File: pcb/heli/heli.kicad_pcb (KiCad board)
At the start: 4 copper layers, 50.6 x 50 mm, 68 parts, among them J1 Batterie, J2 Debug, J4 Servo, J5 Servo, M1 Motor_DC, M2 Motor_DC, Q1 IRLZ44N, Q2 BC547, Q3 IRLZ44N, Q4 BC547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

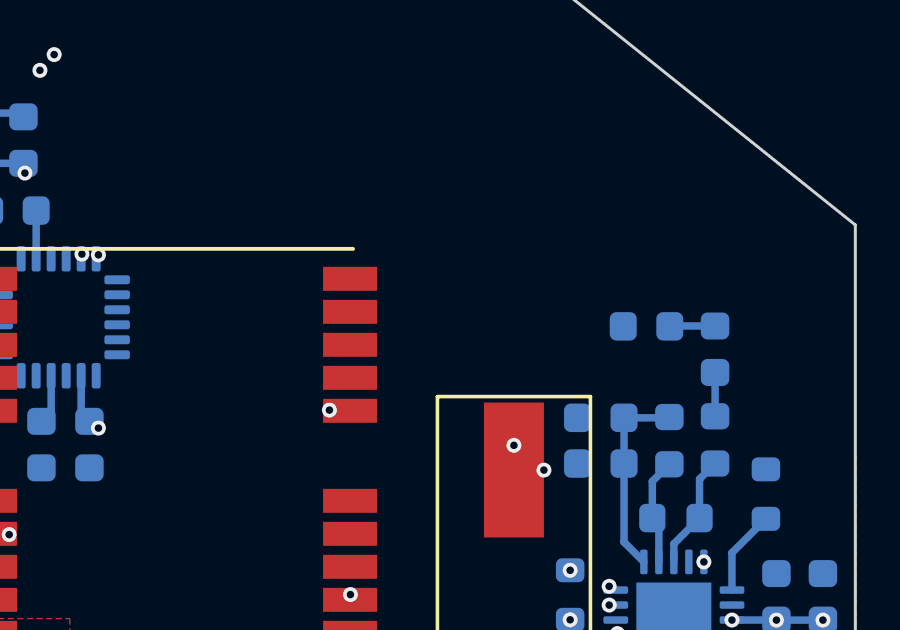
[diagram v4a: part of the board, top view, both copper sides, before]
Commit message: 
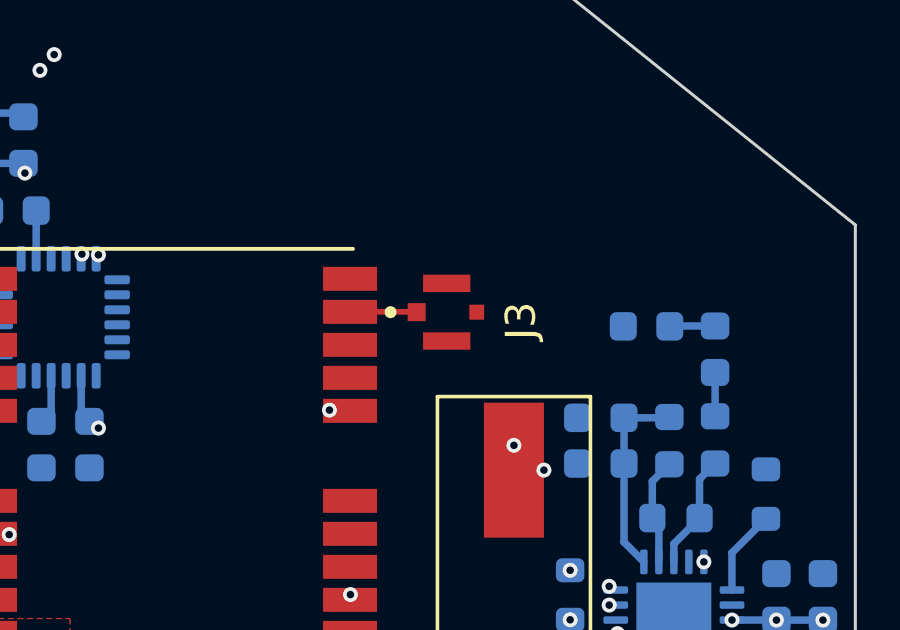
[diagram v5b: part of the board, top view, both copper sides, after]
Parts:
- added J3: CONMHF4-SMD-G-T, lib:LINX_CONMHF4-SMD-G-T, F.Cu at (55.0, 32.8)
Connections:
- U4 pad 11: unconnected-(U4-Pad11) -> Net-(J3-Pad1)
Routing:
- net Net-(J3-Pad1): track 0.00 -> 2.23 mm
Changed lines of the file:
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@@
   (net 70 "unconnected-(U4-Pad6)")
   (net 71 "unconnected-(U4-Pad9)")
-  (net 72 "unconnected-(U4-Pad11)")
+  (net 72 "Net-(J3-Pad1)")
   (net 73 "unconnected-(U4-Pad14)")
   (net 74 "unconnected-(U4-Pad15)")
@@
     )
   )
+  (footprint "lib:LINX_CONMHF4-SMD-G-T" (layer "F.Cu")
+    (at 54.9602 32.7862 -90)
+    (property "MANUFACTURER" "Linx")
+    (property "MAXIMUM_PACKAGE_HEIGHT" "0.6 mm")
+    (property "PARTREV" "A")
+    (property "STANDARD" "Manufacturer Recommendations")
+    (property "Sheetfile" "gps.kicad_sch")
+    (property "Sheetname" "GPS")
+    (attr through_hole)
+    (fp_text reference "J3" (at 0.288 -2.472 90) (layer "F.SilkS")
+      (effects (font (size 1 1) (thickness 0.15)))
+    )
+    (fp_text value "CONMHF4-SMD-G-T" (at 9.559 3.092 90) (layer "F.Fab")
+      (effects (font (size 1 1) (thickness 0.15)))
+    )
+    (fp_circle (center 0 1.873) (end 0.1 1.873) (layer "F.SilkS") (width 0.2) (fill none))
+    (fp_line (start -1.5 -1.5) (end -1.5 1.55) (layer "F.CrtYd") (width 0.05))
+    (fp_line (start 1.5 1.55) (end 1.5 -1.5) (layer "F.CrtYd") (width 0.05))
+    (fp_line (start 1.5 -1.5) (end -1.5 -1.5) (layer "F.CrtYd") (width 0.05))
+    (fp_line (start -1.5 1.55) (end 1.5 1.55) (layer "F.CrtYd") (width 0.05))
+    (fp_line (start -0.88 -0.84) (end -0.88 0.84) (layer "F.Fab") (width 0.127))
+    (fp_line (start -0.88 -0.84) (end 0.58 -0.84) (layer "F.Fab") (width 0.127))
+    (fp_line (start 0.88 0.84) (end 0.88 -0.54) (layer "F.Fab") (width 0.127))
+    (fp_line (start 0.58 -0.84) (end 0.88 -0.54) (layer "F.Fab") (width 0.127))
+    (fp_line (start -0.88 0.84) (end 0.88 0.84) (layer "F.Fab") (width 0.127))
+    (fp_circle (center 0 1.873) (end 0.1 1.873) (layer "F.Fab") (width 0.2) (fill none))
+    (pad "1" smd rect (at 0 1 270) (size 0.6 0.6) (layers "F.Cu" "F.Paste" "F.Mask")
+      (net 72 "Net-(J3-Pad1)") (pintype "passive"))
+    (pad "S1" smd rect (at -0.96 0 270) (size 0.58 1.58) (layers "F.Cu" "F.Paste" "F.Mask")
+      (net 2 "GND") (pintype "passive"))
+    (pad "S2" smd rect (at 0 -1 270) (size 0.5 0.5) (layers "F.Cu" "F.Paste" "F.Mask")
+      (net 2 "GND") (pintype "passive"))
+    (pad "S3" smd rect (at 0.96 0 270) (size 0.58 1.58) (layers "F.Cu" "F.Paste" "F.Mask")
+      (net 2 "GND") (pintype "passive"))
+    (zone (net 0) (net_name "") (layer "F.Cu") (hatch full 0.508)
+      (connect_pads (clearance 0))
+      (min_thickness 0.01)
+      (keepout (tracks not_allowed) (vias not_allowed) (pads not_allowed) (copperpour not_allowed) (footprints allowed))
+      (fill (thermal_gap 0.508) (thermal_bridge_width 0.508))
+      (polygon
+        (pts
+          (xy 55.7102 32.1162)
+          (xy 55.7102 33.4562)
+          (xy 54.2602 33.4562)
+          (xy 54.2602 32.1162)
+        )
+      )
+    )
+    (zone (net 0) (net_name "") (layers *.Cu) (hatch full 0.508)
+      (connect_pads (clearance 0))
+      (min_thickness 0.01)
+      (keepout (tracks allowed) (vias not_allowed) (pads allowed) (copperpour allowed) (footprints allowed))
+      (fill (thermal_gap 0.508) (thermal_bridge_width 0.508))
+      (polygon
+        (pts
+          (xy 55.7102 32.1162)
+          (xy 55.7102 33.4562)
+          (xy 54.2602 33.4562)
+          (xy 54.2602 32.1162)
+        )
+      )
+    )
+    (zone (net 0) (net_name "") (layer "B.Cu") (hatch full 0.508)
+      (connect_pads (clearance 0))
+      (min_thickness 0.01)
+      (keepout (tracks not_allowed) (vias not_allowed) (pads not_allowed) (copperpour not_allowed) (footprints allowed))
+      (fill (thermal_gap 0.508) (thermal_bridge_width 0.508))
+      (polygon
+        (pts
+          (xy 55.7102 32.1162)
+          (xy 55.7102 33.4562)
+          (xy 54.2602 33.4562)
+          (xy 54.2602 32.1162)
+        )
+      )
+    )
+  )
   (footprint "Package_TO_SOT_THT:TO-92_Inline" (layer "F.Cu")
     (at 31 41.1 -90)
@@
       (net 2 "GND") (pinfunction "GND") (pintype "power_in"))
     (pad "11" smd rect (at -6 5.9 180) (size 1.8 0.8) (layers "F.Cu" "F.Mask")
-      (net 72 "unconnected-(U4-Pad11)") (pinfunction "RF_IN") (pintype "input"))
+      (net 72 "Net-(J3-Pad1)") (pinfunction "RF_IN") (pintype "input"))
     (pad "12" smd rect (at -6 7 180) (size 1.8 0.8) (layers "F.Cu" "F.Mask")
       (net 2 "GND") (pinfunction "GND") (pintype "power_in"))
@@
   (segment (start 28.35 27.9) (end 28.35 25.7) (width 0.25) (layer "In2.Cu") (net 51))
   (via micro (at 28.35 25.7) (size 0.5) (drill 0.25) (layers "In2.Cu" "B.Cu") (free) (net 51))
+  (segment (start 51.7375 32.775) (end 53.949 32.775) (width 0.194121) (layer "F.Cu") (net 72))
+  (segment (start 53.949 32.775) (end 53.9602 32.7862) (width 0.25) (layer "F.Cu") (net 72))
   (segment (start 64.4685 43.548) (end 64.923 43.548) (width 0.25) (layer "B.Cu") (net 77))
   (segment (start 64.923 43.548) (end 65.95 44.575) (width 0.25) (layer "B.Cu") (net 77))
@@
   (zone locked (net 10) (net_name "7.4V") (layers "In1.Cu" "In2.Cu") (hatch edge 0.508)
     (priority 1)
-    (connect_pads yes (clearance 0.508))
+    (connect_pads yes (clearance 0.2))
     (min_thickness 0.254) (filled_areas_thickness no)
     (fill yes (thermal_gap 0.508) (thermal_bridge_width 0.508) (smoothing fillet) (radius 2))
